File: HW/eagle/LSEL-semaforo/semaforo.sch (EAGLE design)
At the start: 14 parts, among them J1 RJ11-2L-B, J3 RJ11-2L-B, U1 Tiny45-20-SMT

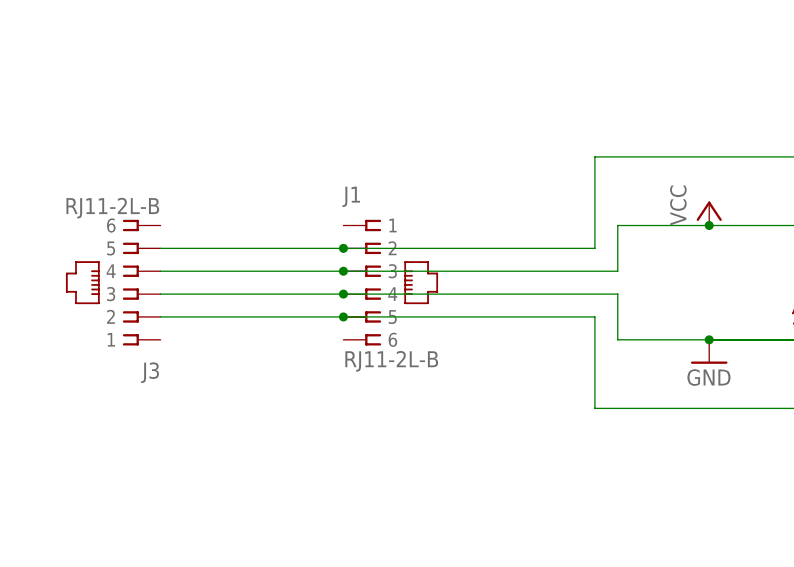
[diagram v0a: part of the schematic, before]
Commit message: Semaforo RJ changed
correction of mistakes
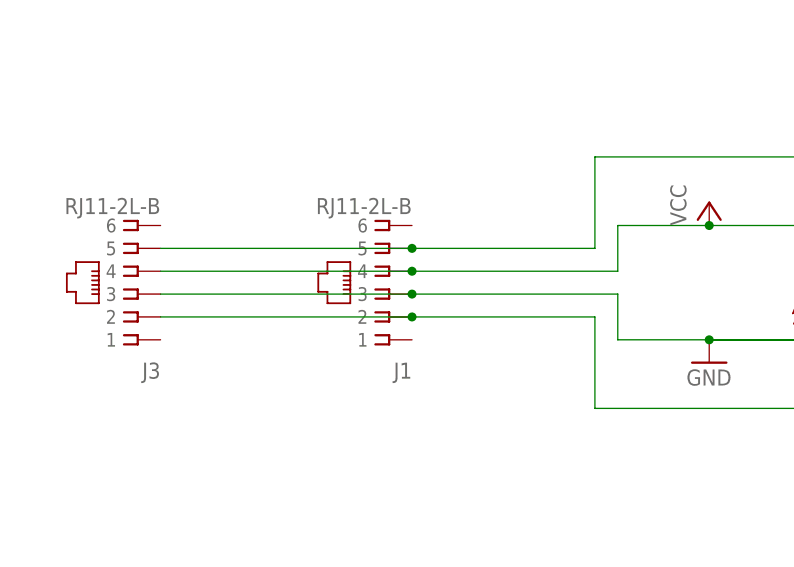
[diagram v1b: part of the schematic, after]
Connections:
- net GND: now also J1.3; no longer J1.4
- net MOSI: now also J1.5; no longer J1.2
- net SCK: now also J1.2; no longer J1.5
- net VCC: now also J1.4; no longer J1.3
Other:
- moved on the sheet: J1
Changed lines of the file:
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@@
 <instance part="P+3" gate="VCC" x="109.22" y="22.86"/>
 <instance part="J3" gate="G$1" x="-48.26" y="38.1" rot="R180"/>
-<instance part="J1" gate="G$1" x="-22.86" y="40.64"/>
+<instance part="J1" gate="G$1" x="-20.32" y="38.1" rot="R180"/>
 </instances>
 <busses>
@@
 <junction x="15.24" y="45.72"/>
 <junction x="38.1" y="45.72"/>
-<wire x1="5.08" y1="40.64" x2="-25.4" y2="40.64" width="0.1524" layer="91"/>
+<wire x1="5.08" y1="40.64" x2="-17.78" y2="40.64" width="0.1524" layer="91"/>
 <pinref part="J3" gate="G$1" pin="4"/>
-<wire x1="-25.4" y1="40.64" x2="-45.72" y2="40.64" width="0.1524" layer="91"/>
-<pinref part="J1" gate="G$1" pin="3"/>
-<junction x="-25.4" y="40.64"/>
+<wire x1="-17.78" y1="40.64" x2="-45.72" y2="40.64" width="0.1524" layer="91"/>
+<pinref part="J1" gate="G$1" pin="4"/>
+<junction x="-17.78" y="40.64"/>
 </segment>
 <segment>
@@
 <pinref part="GND4" gate="1" pin="GND"/>
 <junction x="15.24" y="33.02"/>
-<wire x1="5.08" y1="38.1" x2="-25.4" y2="38.1" width="0.1524" layer="91"/>
+<wire x1="5.08" y1="38.1" x2="-17.78" y2="38.1" width="0.1524" layer="91"/>
 <pinref part="J3" gate="G$1" pin="3"/>
-<wire x1="-25.4" y1="38.1" x2="-45.72" y2="38.1" width="0.1524" layer="91"/>
-<pinref part="J1" gate="G$1" pin="4"/>
-<junction x="-25.4" y="38.1"/>
+<wire x1="-17.78" y1="38.1" x2="-45.72" y2="38.1" width="0.1524" layer="91"/>
+<pinref part="J1" gate="G$1" pin="3"/>
+<junction x="-17.78" y="38.1"/>
 </segment>
 <segment>
@@
 <junction x="91.44" y="40.64"/>
 <label x="99.06" y="40.64" size="1.778" layer="95"/>
-<wire x1="2.54" y1="35.56" x2="-25.4" y2="35.56" width="0.1524" layer="91"/>
+<wire x1="2.54" y1="35.56" x2="-17.78" y2="35.56" width="0.1524" layer="91"/>
 <pinref part="J3" gate="G$1" pin="2"/>
-<wire x1="-25.4" y1="35.56" x2="-45.72" y2="35.56" width="0.1524" layer="91"/>
-<pinref part="J1" gate="G$1" pin="5"/>
-<junction x="-25.4" y="35.56"/>
+<wire x1="-17.78" y1="35.56" x2="-45.72" y2="35.56" width="0.1524" layer="91"/>
+<pinref part="J1" gate="G$1" pin="2"/>
+<junction x="-17.78" y="35.56"/>
 </segment>
 </net>
@@
 <wire x1="2.54" y1="43.18" x2="2.54" y2="53.34" width="0.1524" layer="91"/>
 <wire x1="2.54" y1="53.34" x2="91.44" y2="53.34" width="0.1524" layer="91"/>
-<wire x1="2.54" y1="43.18" x2="-25.4" y2="43.18" width="0.1524" layer="91"/>
+<wire x1="2.54" y1="43.18" x2="-17.78" y2="43.18" width="0.1524" layer="91"/>
 <pinref part="U1" gate="G$1" pin="PB0(MOSI)"/>
-<wire x1="-25.4" y1="43.18" x2="-45.72" y2="43.18" width="0.1524" layer="91"/>
+<wire x1="-17.78" y1="43.18" x2="-45.72" y2="43.18" width="0.1524" layer="91"/>
 <wire x1="91.44" y1="45.72" x2="88.9" y2="45.72" width="0.1524" layer="91"/>
 <label x="99.06" y="45.72" size="1.778" layer="95"/>
@@
 <junction x="91.44" y="45.72"/>
 <pinref part="J3" gate="G$1" pin="5"/>
-<pinref part="J1" gate="G$1" pin="2"/>
-<junction x="-25.4" y="43.18"/>
-</segment>
-</net>
+<pinref part="J1" gate="G$1" pin="5"/>
+<junction x="-17.78" y="43.18"/>
+</segment>
+</net>
